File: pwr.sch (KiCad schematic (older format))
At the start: 12 parts, among them J1 Conn_01x02, U5 MCP73871-xxI_ML

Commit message: More power setup
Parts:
- added C6: 470pF, Capacitors_SMD:C_0805, symbol Device:C_Small
- added C7: 0.1uF, Capacitors_SMD:C_0805, symbol Device:C_Small
- added C8: 4.7uF, Capacitors_SMD:C_0805, symbol Device:C_Small
- added U7: MIC5219-3.3BM5, TO_SOT_Packages_SMD:SOT-23-5, symbol Regulator_Linear:AP131-33
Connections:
- net labels added: +3.3
- wire segments 63 -> 83
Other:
- note added: "3.3V Regulator"
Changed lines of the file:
@@
 Wire Wire Line
 	6300 3750 6950 3750
-Text GLabel 4300 2950 1    50   Input ~ 0
-VBUS
 Wire Wire Line
 	4950 3050 4950 3150
@@
 	1    0    0    -1
 $EndComp
-Text GLabel 4700 2950 1    50   Input ~ 0
-VBUS
-Wire Wire Line
-	4700 2950 4700 3050
 Wire Wire Line
 	4700 3050 4950 3050
@@
 Wire Wire Line
 	4300 3700 4300 3800
-Wire Wire Line
-	4300 3000 4300 2950
 $Comp
 L Device:R R?
@@
 	0    -1   -1   0
 $EndComp
-Text GLabel 3850 2950 1    50   Input ~ 0
-VBUS
-Text GLabel 3500 2950 1    50   Input ~ 0
-VBUS
-Wire Wire Line
-	3850 2950 3850 3000
-Wire Wire Line
-	3500 2950 3500 3000
 Wire Wire Line
 	3500 3300 3500 3400
@@
 Wire Wire Line
 	3500 4100 4700 4100
-Text GLabel 4800 4100 1    50   Input ~ 0
-VBUS
 Wire Wire Line
 	5100 4050 4950 4050
@@
 Wire Wire Line
 	4950 4150 5100 4150
-Wire Wire Line
-	4800 4100 4800 4150
 Wire Wire Line
 	4800 4150 4950 4150
@@
 Wire Wire Line
 	4800 4250 4800 4150
-Connection ~ 4800 4150
 Wire Wire Line
 	5100 4350 4800 4350
@@
 	4800 4350 4800 4250
 Connection ~ 4800 4250
-Text GLabel 6600 2850 1    50   Output ~ 0
-VBAT
 Wire Wire Line
 	6300 3050 6600 3050
 Wire Wire Line
-	6600 3050 6600 2850
-Wire Wire Line
 	6300 3150 6600 3150
 Wire Wire Line
 	6600 3150 6600 3050
-Connection ~ 6600 3050
 Wire Wire Line
 	6300 3550 6400 3550
@@
 	1    0    0    -1
 $EndComp
+Wire Wire Line
+	3500 2550 3500 2800
+Wire Wire Line
+	3500 2800 3850 2800
+Wire Wire Line
+	3850 2800 3850 3000
+Connection ~ 3500 2800
+Wire Wire Line
+	3500 2800 3500 3000
+Wire Wire Line
+	3850 2800 4300 2800
+Wire Wire Line
+	4300 2800 4300 3000
+Connection ~ 3850 2800
+Wire Wire Line
+	4300 2800 4700 2800
+Wire Wire Line
+	4700 2800 4700 3050
+Connection ~ 4300 2800
+Text GLabel 3500 2550 1    50   Input ~ 0
+VBUS
+Text GLabel 4650 4250 0    50   Input ~ 0
+VBUS
+Wire Wire Line
+	4800 4250 4650 4250
+$Comp
+L Regulator_Linear:AP131-33 U7
+U 1 1 5D0EA3C7
+P 4100 5800
+F 0 "U7" H 4100 6142 50  0000 C CNN
+F 1 "MIC5219-3.3BM5" H 4100 6051 50  0000 C CNN
+F 2 "TO_SOT_Packages_SMD:SOT-23-5" H 4100 6125 50  0001 C CNN
+F 3 "http://www.diodes.com/_files/datasheets/AP131.pdf" H 4100 5800 50  0001 C CNN
+	1    4100 5800
+	1    0    0    -1
+$EndComp
+Text Notes 3850 5300 0    50   ~ 0
+3.3V Regulator
+Wire Wire Line
+	6600 3050 7100 3050
+Connection ~ 6600 3050
+Text Label 6950 3050 0    50   ~ 0
+VBAT
+Wire Wire Line
+	3800 5700 3700 5700
+Text Label 3350 5700 0    50   ~ 0
+VBAT
+Wire Wire Line
+	3700 5700 3700 5800
+Wire Wire Line
+	3700 5800 3800 5800
+Connection ~ 3700 5700
+Wire Wire Line
+	3700 5700 3350 5700
+$Comp
+L power:(GND) #PWR04
+U 1 1 5D0F6FB4
+P 4100 6250
+F 0 "#PWR04" H 4100 6250 30  0001 C CNN
+F 1 "(GND)" H 4100 6250 30  0001 C CNN
+F 2 "" H 4100 6250 60  0000 C CNN
+F 3 "" H 4100 6250 60  0000 C CNN
+	1    4100 6250
+	1    0    0    -1
+$EndComp
+Wire Wire Line
+	4100 6100 4100 6250
+$Comp
+L Device:C_Small C?
+U 1 1 5D0F8777
+P 4550 6050
+AR Path="/5D0F8777" Ref="C?"  Part="1"
+AR Path="/5C2799D2/5D0F8777" Ref="C?"  Part="1"
+AR Path="/5D08445F/5D0F8777" Ref="C?"  Part="1"
+AR Path="/5D08BD3C/5D0F8777" Ref="C6"  Part="1"
+F 0 "C6" H 4560 6120 50  0000 L CNN
+F 1 "470pF" H 4560 5970 50  0000 L CNN
+F 2 "Capacitors_SMD:C_0805" H 4550 6050 50  0001 C CNN
+F 3 "" H 4550 6050 50  0000 C CNN
+	1    4550 6050
+	1    0    0    -1
+$EndComp
+Wire Wire Line
+	4550 5800 4550 5950
+Wire Wire Line
+	4400 5800 4550 5800
+$Comp
+L power:(GND) #PWR05
+U 1 1 5D0FB435
+P 4550 6250
+F 0 "#PWR05" H 4550 6250 30  0001 C CNN
+F 1 "(GND)" H 4550 6250 30  0001 C CNN
+F 2 "" H 4550 6250 60  0000 C CNN
+F 3 "" H 4550 6250 60  0000 C CNN
+	1    4550 6250
+	1    0    0    -1
+$EndComp
+Wire Wire Line
+	4550 6150 4550 6250
+Wire Wire Line
+	4400 5700 4900 5700
+Wire Wire Line
+	5250 5700 5250 5600
+$Comp
+L power:+3.3 #PWR07
+U 1 1 5D0FE5DB
+P 5250 5600
+F 0 "#PWR07" H 5250 5650 30  0001 C CNN
+F 1 "+3.3" H 5250 5733 50  0000 C CNN
+F 2 "" H 5250 5600 60  0000 C CNN
+F 3 "" H 5250 5600 60  0000 C CNN
+	1    5250 5600
+	1    0    0    -1
+$EndComp
+$Comp
+L Device:C_Small C?
+U 1 1 5D0FE8A9
+P 4900 6050
+AR Path="/5D0FE8A9" Ref="C?"  Part="1"
+AR Path="/5C2799D2/5D0FE8A9" Ref="C?"  Part="1"
+AR Path="/5D08445F/5D0FE8A9" Ref="C?"  Part="1"
+AR Path="/5D08BD3C/5D0FE8A9" Ref="C7"  Part="1"
+F 0 "C7" H 5000 6050 50  0000 L CNN
+F 1 "0.1uF" H 4850 6150 50  0000 L CNN
+F 2 "Capacitors_SMD:C_0805" H 4900 6050 50  0001 C CNN
+F 3 "" H 4900 6050 50  0000 C CNN
+	1    4900 6050
+	1    0    0    -1
+$EndComp
+$Comp
+L Device:C_Small C?
+U 1 1 5D0FE8E1
+P 5250 6050
+AR Path="/5D0FE8E1" Ref="C?"  Part="1"
+AR Path="/5C2799D2/5D0FE8E1" Ref="C?"  Part="1"
+AR Path="/5D08445F/5D0FE8E1" Ref="C?"  Part="1"
+AR Path="/5D08BD3C/5D0FE8E1" Ref="C8"  Part="1"
+F 0 "C8" H 5350 6050 50  0000 L CNN
+F 1 "4.7uF" H 5200 6150 50  0000 L CNN
+F 2 "Capacitors_SMD:C_0805" H 5250 6050 50  0001 C CNN
+F 3 "" H 5250 6050 50  0000 C CNN
+	1    5250 6050
+	1    0    0    -1
+$EndComp
+$Comp
+L power:(GND) #PWR06
+U 1 1 5D0FEB98
+P 5100 6250
+F 0 "#PWR06" H 5100 6250 30  0001 C CNN
+F 1 "(GND)" H 5100 6250 30  0001 C CNN
+F 2 "" H 5100 6250 60  0000 C CNN
+F 3 "" H 5100 6250 60  0000 C CNN
+	1    5100 6250
+	1    0    0    -1
+$EndComp
+Wire Wire Line
+	4900 6150 5100 6150
+Wire Wire Line
+	5100 6150 5100 6250
+Wire Wire Line
+	5250 6150 5100 6150
+Connection ~ 5100 6150
+Wire Wire Line
+	4900 5950 4900 5700
+Connection ~ 4900 5700
+Wire Wire Line
+	4900 5700 5250 5700
+Wire Wire Line
+	5250 5950 5250 5700
+Connection ~ 5250 5700
 $EndSCHEMATC

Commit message: Connectors
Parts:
- J1: footprint (none) -> my-fp-library:Battery Pads 3x3
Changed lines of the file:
@@
 F 0 "J1" H 7580 3842 50  0000 L CNN
 F 1 "Conn_01x02" H 7580 3751 50  0000 L CNN
-F 2 "" H 7500 3850 50  0001 C CNN
+F 2 "my-fp-library:Battery Pads 3x3" H 7500 3850 50  0001 C CNN
 F 3 "~" H 7500 3850 50  0001 C CNN
 	1    7500 3850

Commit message: New Power_Management from Pin64 schematic.  Much less parts
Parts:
- removed C8: 4.7uF, Capacitors_SMD:C_0805, symbol Device:C_Small
- removed D1: ORANGE, LEDs:LED_0805, symbol Device:LED
- removed D2: GREEN, LEDs:LED_0805, symbol Device:LED
- removed J1: Conn_01x02, my-fp-library:Battery Pads 3x3, symbol Connector_Generic:Conn_01x02
- removed R10: 10K, Resistors_SMD:R_0805, symbol Device:R
- removed R8: 100K, Resistors_SMD:R_0805, symbol Device:R
- removed R9: 1K, Resistors_SMD:R_0805, symbol Device:R
- removed U5: MCP73871-xxI_ML, Housings_DFN_QFN:UQFN-20-1EP_4x4mm_Pitch0.5mm, symbol Microchip:MCP73871-xxI_ML
- removed U7: MIC5219-3.3BM5, TO_SOT_Packages_SMD:SOT-23-5, symbol Regulator_Linear:AP131-33
- added U5: SGM2036_UTDFN, symbol Power_Management:SGM2036_UTDFN
- added U7: SGM40561, symbol Power_Management:SGM40561
- C3: value 10uF -> 1uF
- C6: value 470pF -> 0.1uF
- C7: value 0.1uF -> 1uF
- R4, R5: value 1K -> 100K
- R6: value 270K -> 3M
- R7: value 100K -> 301K
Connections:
- net labels added: VCC, VIN
- net labels removed: +3.3, PWR_SENSE, STAT
- wire segments 83 -> 36
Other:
- note added: "Single-cell Li-Ion battery charger"
- note removed: "Charge Rate = 1000V/PROG1\n1.0K = 1000mA\n2.0K = 500mA"

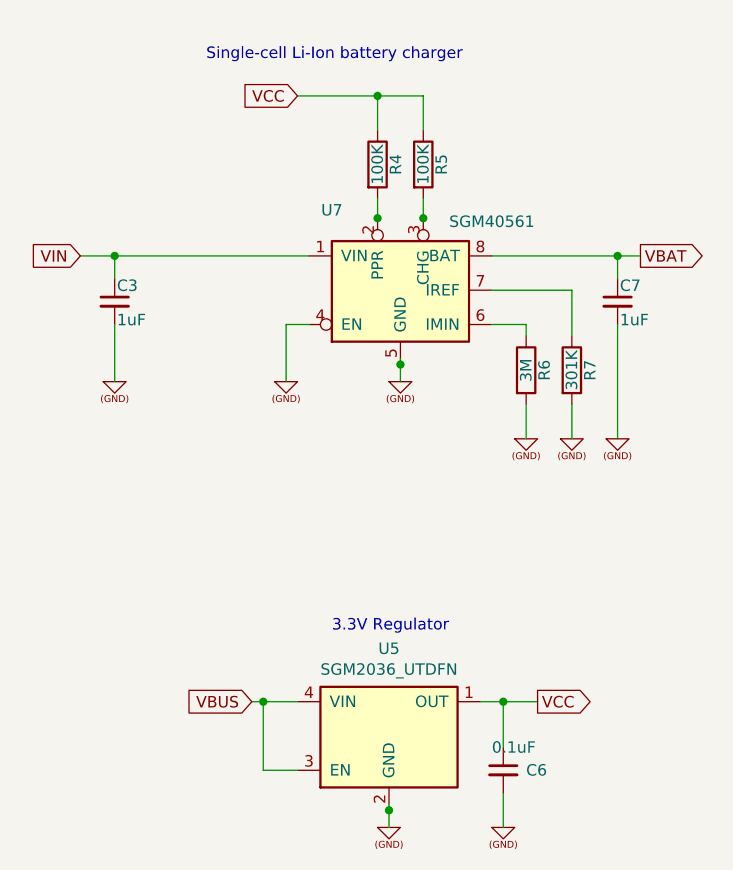
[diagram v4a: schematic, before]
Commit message: Implement 240x240 IPS display
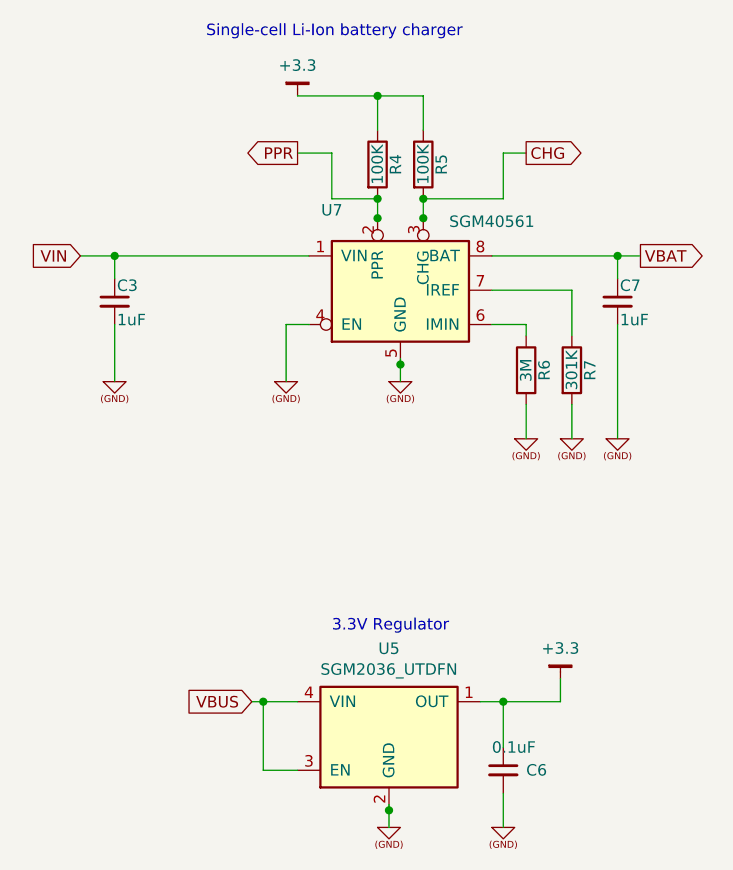
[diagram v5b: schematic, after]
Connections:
- net labels added: +3.3, CHG, PPR
- net labels removed: VCC
- wire segments 36 -> 43
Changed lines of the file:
@@
 $Descr A4 11693 8268
 encoding utf-8
-Sheet 3 4
+Sheet 3 5
 Title ""
 Date ""
@@
 Wire Wire Line
 	5400 4450 5400 4600
-Text GLabel 4200 3100 0    50   Input ~ 0
-VCC
 Wire Wire Line
 	4200 3100 4550 3100
@@
 Wire Wire Line
 	4600 6225 4600 6300
-Text GLabel 5250 5750 2    50   Output ~ 0
-VCC
 Wire Wire Line
 	5000 5750 5100 5750
@@
 	5100 5950 5100 5750
 Connection ~ 5100 5750
-Wire Wire Line
-	5100 5750 5250 5750
 $Comp
 L power:(GND) #PWR016
@@
 Text Notes 4350 5450 0    50   ~ 0
 3.3V Regulator
-Text Notes 3800 2950 0    50   ~ 0
+Text Notes 3800 2850 0    50   ~ 0
 Single-cell Li-Ion battery charger
+$Comp
+L power:+3.3 #PWR0106
+U 1 1 5DA4537A
+P 5350 5650
+F 0 "#PWR0106" H 5350 5700 30  0001 C CNN
+F 1 "+3.3" H 5350 5783 50  0000 C CNN
+F 2 "" H 5350 5650 60  0000 C CNN
+F 3 "" H 5350 5650 60  0000 C CNN
+	1    5350 5650
+	1    0    0    -1
+$EndComp
+Wire Wire Line
+	5350 5750 5350 5650
+Wire Wire Line
+	5100 5750 5350 5750
+Text GLabel 4200 3350 0    50   Output ~ 0
+PPR
+Text GLabel 5200 3350 2    50   Output ~ 0
+CHG
+Wire Wire Line
+	4550 3550 4350 3550
+Wire Wire Line
+	4350 3550 4350 3350
+Wire Wire Line
+	4350 3350 4200 3350
+Connection ~ 4550 3550
+Wire Wire Line
+	4750 3550 5100 3550
+Wire Wire Line
+	5100 3550 5100 3350
+Wire Wire Line
+	5100 3350 5200 3350
+Connection ~ 4750 3550
+$Comp
+L power:+3.3 #PWR0108
+U 1 1 5DA481CF
+P 4200 3100
+F 0 "#PWR0108" H 4200 3150 30  0001 C CNN
+F 1 "+3.3" H 4200 3233 50  0000 C CNN
+F 2 "" H 4200 3100 60  0000 C CNN
+F 3 "" H 4200 3100 60  0000 C CNN
+	1    4200 3100
+	1    0    0    -1
+$EndComp
 $EndSCHEMATC

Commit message: Power board PCB
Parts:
- added D1: ZLLS410, Diodes_SMD:D_SOD-323, symbol _semi:DIODE
- added J6: Conn_01x02, my-fp-library:Battery Pads 3x3, symbol Connector_Generic:Conn_01x02
- added Q2: FDC6420C, TO_SOT_Packages_SMD:SOT-666, symbol mosfet:FDC6420C
- U7: footprint (none) -> Housings_DFN_QFN:VDFN-8-1EP_2x2mm_Pitch0.5mm
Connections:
- net labels added: +3.3V, +5
- net labels removed: +3.3, VBAT, VBUS
- wire segments 43 -> 56
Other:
- note added: "BATT"
- moved on the sheet: C3, C7
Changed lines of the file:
@@
 F 0 "U7" H 4350 4600 50  0000 C CNN
 F 1 "SGM40561" H 5050 4550 50  0000 C CNN
-F 2 "" H 4650 4100 50  0001 C CNN
+F 2 "Housings_DFN_QFN:VDFN-8-1EP_2x2mm_Pitch0.5mm" H 4650 4100 50  0001 C CNN
 F 3 "" H 4650 4100 50  0001 C CNN
 	1    4650 4100
@@
 L Device:C_Small C?
 U 1 1 5D99312F
-P 3400 4000
+P 3400 4200
 AR Path="/5D99312F" Ref="C?"  Part="1"
 AR Path="/5C2799D2/5D99312F" Ref="C?"  Part="1"
 AR Path="/5D08445F/5D99312F" Ref="C?"  Part="1"
 AR Path="/5D08BD3C/5D99312F" Ref="C3"  Part="1"
-F 0 "C3" H 3410 4070 50  0000 L CNN
-F 1 "1uF" H 3410 3920 50  0000 L CNN
-F 2 "Capacitors_SMD:C_0805" H 3400 4000 50  0001 C CNN
-F 3 "" H 3400 4000 50  0000 C CNN
-	1    3400 4000
+F 0 "C3" H 3410 4270 50  0000 L CNN
+F 1 "1uF" H 3410 4120 50  0000 L CNN
+F 2 "Capacitors_SMD:C_0805" H 3400 4200 50  0001 C CNN
+F 3 "" H 3400 4200 50  0000 C CNN
+	1    3400 4200
 	1    0    0    -1
 $EndComp
@@
 	3250 3800 3400 3800
 Wire Wire Line
-	3400 3900 3400 3800
+	3400 4100 3400 3800
 Connection ~ 3400 3800
-Wire Wire Line
-	3400 3800 4250 3800
 $Comp
 L power:(GND) #PWR04
 U 1 1 5D99D2A3
-P 3400 4350
-F 0 "#PWR04" H 3400 4350 30  0001 C CNN
-F 1 "(GND)" H 3400 4350 30  0001 C CNN
-F 2 "" H 3400 4350 60  0000 C CNN
-F 3 "" H 3400 4350 60  0000 C CNN
-	1    3400 4350
-	1    0    0    -1
-$EndComp
-Wire Wire Line
-	3400 4100 3400 4350
+P 3400 4550
+F 0 "#PWR04" H 3400 4550 30  0001 C CNN
+F 1 "(GND)" H 3400 4550 30  0001 C CNN
+F 2 "" H 3400 4550 60  0000 C CNN
+F 3 "" H 3400 4550 60  0000 C CNN
+	1    3400 4550
+	1    0    0    -1
+$EndComp
+Wire Wire Line
+	3400 4300 3400 4550
 $Comp
 L power:(GND) #PWR05
 U 1 1 5D9A0796
-P 4150 4350
-F 0 "#PWR05" H 4150 4350 30  0001 C CNN
-F 1 "(GND)" H 4150 4350 30  0001 C CNN
-F 2 "" H 4150 4350 60  0000 C CNN
-F 3 "" H 4150 4350 60  0000 C CNN
-	1    4150 4350
+P 4150 4600
+F 0 "#PWR05" H 4150 4600 30  0001 C CNN
+F 1 "(GND)" H 4150 4600 30  0001 C CNN
+F 2 "" H 4150 4600 60  0000 C CNN
+F 3 "" H 4150 4600 60  0000 C CNN
+	1    4150 4600
 	1    0    0    -1
 $EndComp
@@
 	4250 4100 4150 4100
 Wire Wire Line
-	4150 4100 4150 4350
+	4150 4100 4150 4600
 Wire Wire Line
 	5050 3800 5600 3800
-Text GLabel 5700 3800 2    50   Output ~ 0
-VBAT
 $Comp
 L Device:C_Small C?
 U 1 1 5D9A6502
-P 5600 4000
+P 5600 4300
 AR Path="/5D9A6502" Ref="C?"  Part="1"
 AR Path="/5C2799D2/5D9A6502" Ref="C?"  Part="1"
 AR Path="/5D08445F/5D9A6502" Ref="C?"  Part="1"
 AR Path="/5D08BD3C/5D9A6502" Ref="C7"  Part="1"
-F 0 "C7" H 5610 4070 50  0000 L CNN
-F 1 "1uF" H 5610 3920 50  0000 L CNN
-F 2 "Capacitors_SMD:C_0805" H 5600 4000 50  0001 C CNN
-F 3 "" H 5600 4000 50  0000 C CNN
-	1    5600 4000
+F 0 "C7" H 5610 4370 50  0000 L CNN
+F 1 "1uF" H 5610 4220 50  0000 L CNN
+F 2 "Capacitors_SMD:C_0805" H 5600 4300 50  0001 C CNN
+F 3 "" H 5600 4300 50  0000 C CNN
+	1    5600 4300
 	1    0    0    -1
 $EndComp
@@
 $EndComp
 Wire Wire Line
-	5600 3900 5600 3800
-Connection ~ 5600 3800
-Wire Wire Line
-	5600 3800 5700 3800
-Wire Wire Line
-	5600 4100 5600 4600
+	5600 4200 5600 3800
+Wire Wire Line
+	5600 4400 5600 4600
 $Comp
 L power:(GND) #PWR07
 U 1 1 5D9B1226
-P 4650 4350
-F 0 "#PWR07" H 4650 4350 30  0001 C CNN
-F 1 "(GND)" H 4650 4350 30  0001 C CNN
-F 2 "" H 4650 4350 60  0000 C CNN
-F 3 "" H 4650 4350 60  0000 C CNN
-	1    4650 4350
+P 4650 4600
+F 0 "#PWR07" H 4650 4600 30  0001 C CNN
+F 1 "(GND)" H 4650 4600 30  0001 C CNN
+F 2 "" H 4650 4600 60  0000 C CNN
+F 3 "" H 4650 4600 60  0000 C CNN
+	1    4650 4600
 	1    0    0    -1
 $EndComp
@@
 Connection ~ 4650 4275
 Wire Wire Line
-	4650 4275 4650 4350
+	4650 4275 4650 4600
 $Comp
 L Device:R R?
@@
 Wire Wire Line
 	5400 4450 5400 4600
-Wire Wire Line
-	4200 3100 4550 3100
 $Comp
 L Device:R R?
@@
 	1    0    0    -1
 $EndComp
-Text GLabel 4000 5750 0    50   Input ~ 0
-VBUS
-Wire Wire Line
-	4000 5750 4050 5750
 Wire Wire Line
 	4200 6050 4050 6050
-Wire Wire Line
-	4050 6050 4050 5750
-Connection ~ 4050 5750
-Wire Wire Line
-	4050 5750 4200 5750
 $Comp
 L power:(GND) #PWR06
@@
 Text Notes 3800 2850 0    50   ~ 0
 Single-cell Li-Ion battery charger
-$Comp
-L power:+3.3 #PWR0106
-U 1 1 5DA4537A
-P 5350 5650
-F 0 "#PWR0106" H 5350 5700 30  0001 C CNN
-F 1 "+3.3" H 5350 5783 50  0000 C CNN
-F 2 "" H 5350 5650 60  0000 C CNN
-F 3 "" H 5350 5650 60  0000 C CNN
-	1    5350 5650
-	1    0    0    -1
-$EndComp
-Wire Wire Line
-	5350 5750 5350 5650
-Wire Wire Line
-	5100 5750 5350 5750
 Text GLabel 4200 3350 0    50   Output ~ 0
 PPR
@@
 Connection ~ 4750 3550
 $Comp
-L power:+3.3 #PWR0108
-U 1 1 5DA481CF
-P 4200 3100
-F 0 "#PWR0108" H 4200 3150 30  0001 C CNN
-F 1 "+3.3" H 4200 3233 50  0000 C CNN
-F 2 "" H 4200 3100 60  0000 C CNN
-F 3 "" H 4200 3100 60  0000 C CNN
-	1    4200 3100
-	1    0    0    -1
-$EndComp
+L Connector_Generic:Conn_01x02 J6
+U 1 1 5DA5855D
+P 6150 4100
+F 0 "J6" H 6230 4092 50  0000 L CNN
+F 1 "Conn_01x02" H 6230 4001 50  0000 L CNN
+F 2 "my-fp-library:Battery Pads 3x3" H 6150 4100 50  0001 C CNN
+F 3 "~" H 6150 4100 50  0001 C CNN
+	1    6150 4100
+	1    0    0    -1
+$EndComp
+$Comp
+L power:(GND) #PWR0127
+U 1 1 5DA66F11
+P 5950 4600
+F 0 "#PWR0127" H 5950 4600 30  0001 C CNN
+F 1 "(GND)" H 5950 4600 30  0001 C CNN
+F 2 "" H 5950 4600 60  0000 C CNN
+F 3 "" H 5950 4600 60  0000 C CNN
+	1    5950 4600
+	1    0    0    -1
+$EndComp
+Text Notes 6100 4000 0    50   ~ 0
+BATT
+Wire Wire Line
+	5950 4200 5950 4600
+Wire Wire Line
+	5600 3800 5950 3800
+Wire Wire Line
+	5950 3800 5950 4100
+Connection ~ 5600 3800
+$Comp
+L mosfet:FDC6420C Q2
+U 2 1 5DA8F1C3
+P 6850 3900
+F 0 "Q2" V 7178 3900 50  0000 C CNN
+F 1 "FDC6420C" V 7087 3900 50  0000 C CNN
+F 2 "TO_SOT_Packages_SMD:SOT-666" H 7050 3825 50  0001 L CNN
+F 3 "http://www.irf.com/product-info/datasheets/data/irf7309ipbf.pdf" H 6850 3900 50  0001 L CNN
+	2    6850 3900
+	0    -1   -1   0
+$EndComp
+Wire Wire Line
+	5950 3800 6650 3800
+Connection ~ 5950 3800
+Wire Wire Line
+	3850 3800 3850 4800
+Wire Wire Line
+	3850 4800 6850 4800
+Wire Wire Line
+	6850 4800 6850 4100
+Wire Wire Line
+	3400 3800 3850 3800
+Connection ~ 3850 3800
+Wire Wire Line
+	3850 3800 4250 3800
+$Comp
+L _semi:DIODE D1
+U 1 1 5DA73D2A
+P 7300 4250
+F 0 "D1" H 7220 4204 50  0000 R CNN
+F 1 "ZLLS410" H 7220 4295 50  0000 R CNN
+F 2 "Diodes_SMD:D_SOD-323" H 7300 4250 60  0001 C CNN
+F 3 "" H 7300 4250 60  0000 C CNN
+	1    7300 4250
+	-1   0    0    1
+$EndComp
+Wire Wire Line
+	6850 4800 7300 4800
+Wire Wire Line
+	7300 4800 7300 4350
+Connection ~ 6850 4800
+Wire Wire Line
+	7300 4150 7300 3800
+Wire Wire Line
+	7300 3800 7050 3800
+Wire Wire Line
+	7300 3800 7600 3800
+Connection ~ 7300 3800
+Wire Wire Line
+	7600 3800 7600 3700
+$Comp
+L power:+5 #PWR023
+U 1 1 5DA78201
+P 7600 3700
+F 0 "#PWR023" H 7600 3750 30  0001 C CNN
+F 1 "+5" H 7600 3833 50  0000 C CNN
+F 2 "" H 7600 3700 60  0000 C CNN
+F 3 "" H 7600 3700 60  0000 C CNN
+	1    7600 3700
+	1    0    0    -1
+$EndComp
+$Comp
+L power:+5 #PWR022
+U 1 1 5DA790D1
+P 3850 5700
+F 0 "#PWR022" H 3850 5750 30  0001 C CNN
+F 1 "+5" H 3850 5833 50  0000 C CNN
+F 2 "" H 3850 5700 60  0000 C CNN
+F 3 "" H 3850 5700 60  0000 C CNN
+	1    3850 5700
+	1    0    0    -1
+$EndComp
+Wire Wire Line
+	3850 5700 3850 5750
+Wire Wire Line
+	3850 5750 4050 5750
+Wire Wire Line
+	4050 6050 4050 5750
+Connection ~ 4050 5750
+Wire Wire Line
+	4050 5750 4200 5750
+Text GLabel 5450 5750 2    50   Output ~ 0
++3.3V
+Wire Wire Line
+	5100 5750 5450 5750
+Text GLabel 4100 3100 0    50   Output ~ 0
++3.3V
+Wire Wire Line
+	4100 3100 4550 3100
 $EndSCHEMATC

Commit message: Build power board
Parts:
- added J7: Conn_01x05, Pin_Headers:Pin_Header_Straight_1x05_Pitch2.54mm, symbol Connector_Generic:Conn_01x05
- Q2: footprint TO_SOT_Packages_SMD:SOT-666 -> TO_SOT_Packages_SMD:SuperSOT-6
- U5: footprint (none) -> TO_SOT_Packages_SMD:SOT-23-5
- U7: footprint Housings_DFN_QFN:VDFN-8-1EP_2x2mm_Pitch0.5mm -> Housings_DFN_QFN:TDFN-2x2-8L
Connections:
- wire segments 56 -> 62
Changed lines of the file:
@@
 F 0 "U7" H 4350 4600 50  0000 C CNN
 F 1 "SGM40561" H 5050 4550 50  0000 C CNN
-F 2 "Housings_DFN_QFN:VDFN-8-1EP_2x2mm_Pitch0.5mm" H 4650 4100 50  0001 C CNN
+F 2 "Housings_DFN_QFN:TDFN-2x2-8L" H 4650 4100 50  0001 C CNN
 F 3 "" H 4650 4100 50  0001 C CNN
 	1    4650 4100
@@
 F 0 "U5" H 4600 6582 50  0000 C CNN
 F 1 "SGM2036_UTDFN" H 4600 6491 50  0000 C CNN
-F 2 "" H 4600 6050 50  0001 C CNN
+F 2 "TO_SOT_Packages_SMD:SOT-23-5" H 4600 6050 50  0001 C CNN
 F 3 "" H 4600 6050 50  0001 C CNN
 	1    4600 6050
@@
 F 0 "Q2" V 7178 3900 50  0000 C CNN
 F 1 "FDC6420C" V 7087 3900 50  0000 C CNN
-F 2 "TO_SOT_Packages_SMD:SOT-666" H 7050 3825 50  0001 L CNN
+F 2 "TO_SOT_Packages_SMD:SuperSOT-6" H 7050 3825 50  0001 L CNN
 F 3 "http://www.irf.com/product-info/datasheets/data/irf7309ipbf.pdf" H 6850 3900 50  0001 L CNN
 	2    6850 3900
@@
 Wire Wire Line
 	4100 3100 4550 3100
+Text GLabel 6950 5650 0    50   Input ~ 0
+VIN
+$Comp
+L power:(GND) #PWR024
+U 1 1 5DA84AA6
+P 6950 6100
+F 0 "#PWR024" H 6950 6100 30  0001 C CNN
+F 1 "(GND)" H 6950 6100 30  0001 C CNN
+F 2 "" H 6950 6100 60  0000 C CNN
+F 3 "" H 6950 6100 60  0000 C CNN
+	1    6950 6100
+	1    0    0    -1
+$EndComp
+Text GLabel 6950 5450 0    50   Output ~ 0
++3.3V
+Text GLabel 6950 5550 0    50   Output ~ 0
+CHG
+Text GLabel 6950 5750 0    50   Output ~ 0
+PPR
+$Comp
+L Connector_Generic:Conn_01x05 J7
+U 1 1 5DA87273
+P 7350 5650
+F 0 "J7" H 7430 5692 50  0000 L CNN
+F 1 "Conn_01x05" H 7430 5601 50  0000 L CNN
+F 2 "Pin_Headers:Pin_Header_Straight_1x05_Pitch2.54mm" H 7350 5650 50  0001 C CNN
+F 3 "~" H 7350 5650 50  0001 C CNN
+	1    7350 5650
+	1    0    0    -1
+$EndComp
+Wire Wire Line
+	7150 5850 6950 5850
+Wire Wire Line
+	6950 5850 6950 6100
+Wire Wire Line
+	7150 5750 6950 5750
+Wire Wire Line
+	7150 5650 6950 5650
+Wire Wire Line
+	7150 5550 6950 5550
+Wire Wire Line
+	7150 5450 6950 5450
 $EndSCHEMATC
